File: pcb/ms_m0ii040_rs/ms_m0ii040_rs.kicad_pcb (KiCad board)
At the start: 2 copper layers, 228.6 x 77.7 mm, 100 parts, among them J1 USB_C_Receptacle_USB2.0, J2 Conn_ARM_JTAG_SWD_10, SW1 ESC, SW10 O, SW11 P, SW12 BS, SW13 CTRL, SW14 A, SW15 S, SW16 D, SW17 F, SW18 G, SW19 H, SW2 Q, SW20 J, SW21 K, SW22 L, SW23 ENT, SW25 SHIFT, SW26 Z, SW27 X, SW28 C, SW29 V, SW3 W, SW30 B, SW31 N, SW32 M, SW33 ,, SW34 ., SW35 SHIFT, SW38 WIN, SW39 ALT, SW4 E, SW40 BS, SW42 SPC, SW43 ALT, SW44 APP, SW5 R, SW6 T, SW7 Y, SW8 U, SW9 I, U1 STM32F072C8Tx, U2 TLV73333PDBV

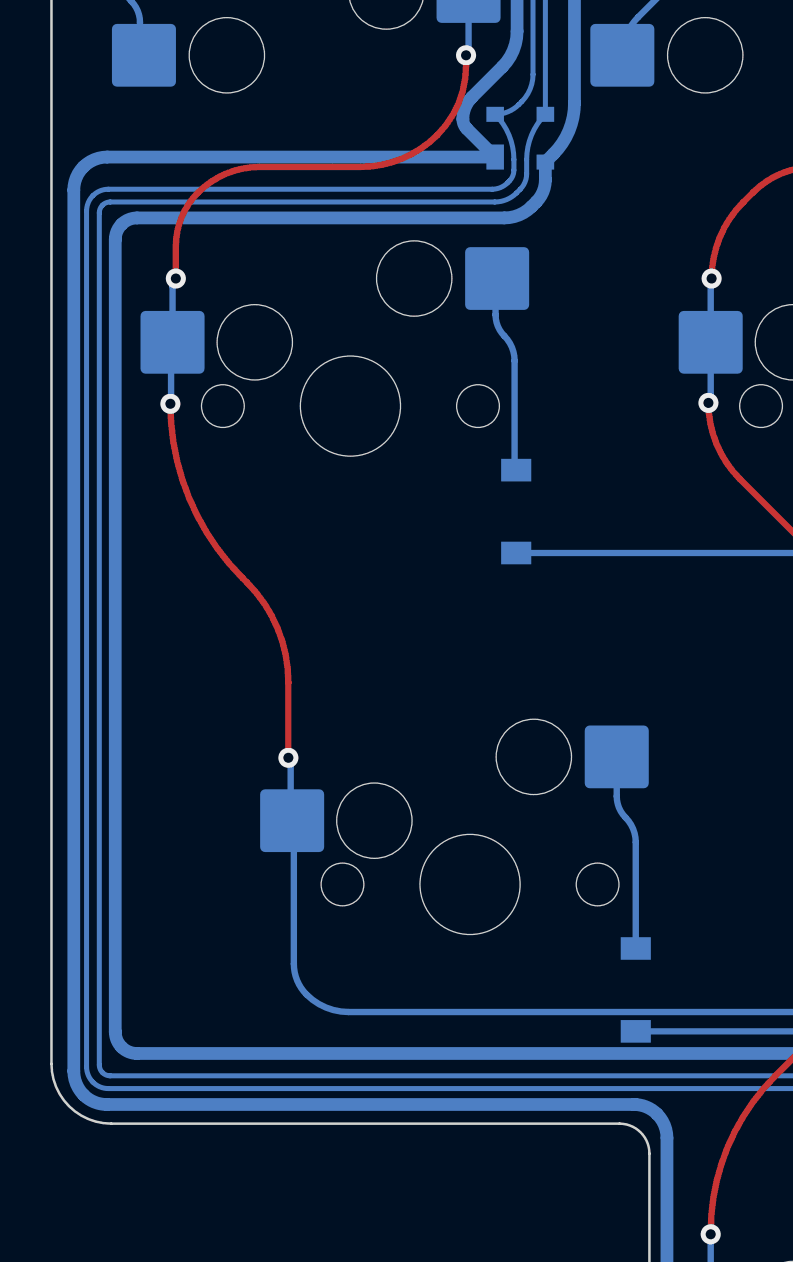
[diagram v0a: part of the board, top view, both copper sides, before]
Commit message: D- and GND slightly separated.
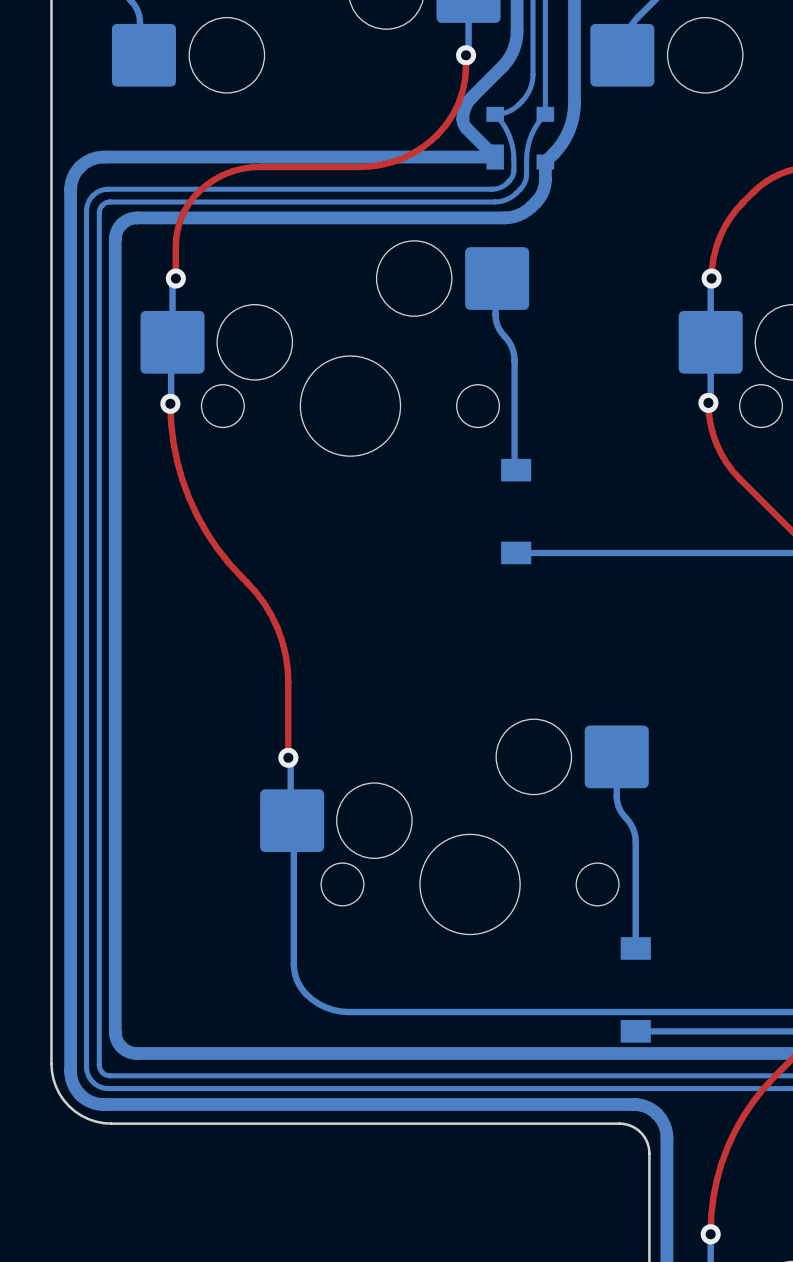
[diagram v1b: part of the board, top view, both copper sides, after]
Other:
- board text added: "M0ii040 Row-staggered rev1.0.2 Copyright marksard 2023. Licensed under CERN-OHL-P v2"
- board text removed: "M0ii040 Row-staggered rev1.0.1 Copyright marksard 2023. Licensed under CERN-OHL-P v2"
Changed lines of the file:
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@@
   (title_block
     (title "m0ii040_rs")
-    (date "2023-03-04")
-    (rev "1.0.1")
+    (date "2023-03-21")
+    (rev "1.0.2")
   )
   (layers
@@
     )
   )
-  (gr_text "M0ii040 Row-staggered rev1.0.1\nCopyright marksard 2023. Licensed under CERN-OHL-P v2\n" (at 215.36025 83.21675) (layer "B.SilkS")
+  (gr_text "M0ii040 Row-staggered rev1.0.2\nCopyright marksard 2023. Licensed under CERN-OHL-P v2\n" (at 215.36025 83.21675) (layer "B.SilkS")
     (effects (font (size 1.5 1.5) (thickness 0.3)) (justify mirror))
   )
@@
   (segment (start 146.474702 111.35995) (end 148.12645 111.35995) (width 0.254) (layer "B.Cu") (net 2))
   (segment (start 139.28725 120.55475) (end 142.93402 120.55475) (width 0.508) (layer "B.Cu") (net 2))
+  (segment (start 48.62525 63.90075) (end 33.048035 63.90075) (width 0.508) (layer "B.Cu") (net 2))
   (segment (start 143.35125 116.84375) (end 143.35125 118.321046) (width 0.508) (layer "B.Cu") (net 2))
   (segment (start 102.177102 110.19155) (end 105.019236 110.19155) (width 0.508) (layer "B.Cu") (net 2))
@@
   (segment (start 134.244447 117.373368) (end 134.104683 117.513132) (width 0.508) (layer "B.Cu") (net 2))
   (segment (start 101.224447 109.796948) (end 101.18725 109.75975) (width 0.508) (layer "B.Cu") (net 2))
-  (segment (start 33.158065 101.63175) (end 54.21904 101.63175) (width 0.508) (layer "B.Cu") (net 2))
   (segment (start 151.8 111.478125) (end 150.680317 111.478125) (width 0.254) (layer "B.Cu") (net 2))
   (segment (start 46.70425 53.37175) (end 46.693052 53.360552) (width 0.508) (layer "B.Cu") (net 2))
@@
   (segment (start 142.93402 120.55475) (end 156.05125 120.55475) (width 0.508) (layer "B.Cu") (net 2))
   (segment (start 145.3875 114.890625) (end 145.3875 112.512983) (width 0.254) (layer "B.Cu") (net 2))
-  (segment (start 48.62525 63.90075) (end 33.175035 63.90075) (width 0.508) (layer "B.Cu") (net 2))
   (segment (start 100.67925 108.53333) (end 100.67925 108.079086) (width 0.508) (layer "B.Cu") (net 2))
   (segment (start 55.46725 119.212965) (end 55.45525 119.224965) (width 0.508) (layer "B.Cu") (net 2))
@@
   (segment (start 151.8 111.478125) (end 153.797191 111.478125) (width 0.254) (layer "B.Cu") (net 2))
   (segment (start 109.129263 120.105737) (end 109.18825 120.04675) (width 0.508) (layer "B.Cu") (net 2))
-  (segment (start 31.84525 65.213565) (end 31.84525 100.301965) (width 0.508) (layer "B.Cu") (net 2))
+  (segment (start 31.71825 65.213565) (end 31.71825 100.301965) (width 0.508) (layer "B.Cu") (net 2))
   (segment (start 149.8875 107.532103) (end 149.8875 106.565625) (width 0.254) (layer "B.Cu") (net 2))
   (segment (start 149.8875 106.565625) (end 149.8875 105.837523) (width 0.254) (layer "B.Cu") (net 2))
@@
   (segment (start 190.34125 118.77675) (end 193.58551 115.53249) (width 0.508) (layer "B.Cu") (net 2))
   (segment (start 100.67925 108.079086) (end 102.673843 108.079086) (width 0.508) (layer "B.Cu") (net 2))
+  (segment (start 33.031065 101.63175) (end 54.21904 101.63175) (width 0.508) (layer "B.Cu") (net 2))
   (segment (start 109.80146 108.23575) (end 141.147841 108.23575) (width 0.508) (layer "B.Cu") (net 2))
   (segment (start 143.475 108.478125) (end 141.732985 108.478125) (width 0.254) (layer "B.Cu") (net 2))
@@
   (arc (start 153.797191 111.478125) (mid 153.848637 111.467891) (end 153.89225 111.43875) (width 0.254) (layer "B.Cu") (net 2))
   (arc (start 141.147841 108.23575) (mid 141.240606 108.254203) (end 141.31925 108.30675) (width 0.508) (layer "B.Cu") (net 2))
-  (arc (start 31.84525 100.301965) (mid 31.947388 100.815444) (end 32.23825 101.25075) (width 0.508) (layer "B.Cu") (net 2))
-  (arc (start 32.22625 64.29375) (mid 31.944276 64.715765) (end 31.84525 65.213565) (width 0.508) (layer "B.Cu") (net 2))
+  (arc (start 31.71825 100.301965) (mid 31.820388 100.815444) (end 32.11125 101.25075) (width 0.508) (layer "B.Cu") (net 2))
+  (arc (start 32.09925 64.29375) (mid 31.817276 64.715765) (end 31.71825 65.213565) (width 0.508) (layer "B.Cu") (net 2))
   (arc (start 183.514065 116.74475) (mid 184.279439 116.592508) (end 184.928291 116.158958) (width 0.508) (layer "B.Cu") (net 2))
   (arc (start 140.90202 120.55475) (mid 141.897621 120.356712) (end 142.74165 119.79275) (width 0.508) (layer "B.Cu") (net 2))
@@
   (arc (start 149.19325 110.85195) (mid 149.34364 110.626875) (end 149.39645 110.361382) (width 0.254) (layer "B.Cu") (net 2))
   (arc (start 141.732985 108.478125) (mid 141.509073 108.433586) (end 141.31925 108.30675) (width 0.254) (layer "B.Cu") (net 2))
-  (arc (start 32.23825 101.25075) (mid 32.660265 101.532735) (end 33.158065 101.63175) (width 0.508) (layer "B.Cu") (net 2))
+  (arc (start 32.11125 101.25075) (mid 32.533265 101.532735) (end 33.031065 101.63175) (width 0.508) (layer "B.Cu") (net 2))
   (arc (start 138.429065 120.04675) (mid 138.147083 119.624735) (end 138.048065 119.126935) (width 0.508) (layer "B.Cu") (net 2))
   (arc (start 149.70125 107.98175) (mid 149.839096 107.77545) (end 149.8875 107.532103) (width 0.254) (layer "B.Cu") (net 2))
@@
   (arc (start 187.225237 119.089737) (mid 187.722586 119.422055) (end 188.30925 119.53875) (width 0.508) (layer "B.Cu") (net 2))
   (arc (start 109.56925 119.03075) (mid 109.732622 118.209421) (end 110.197868 117.513132) (width 0.508) (layer "B.Cu") (net 2))
-  (arc (start 33.175035 63.90075) (mid 32.661556 64.002888) (end 32.22625 64.29375) (width 0.508) (layer "B.Cu") (net 2))
+  (arc (start 33.048035 63.90075) (mid 32.534556 64.002888) (end 32.09925 64.29375) (width 0.508) (layer "B.Cu") (net 2))
   (arc (start 145.12925 116.49075) (mid 144.738249 116.752009) (end 144.277033 116.84375) (width 0.254) (layer "B.Cu") (net 2))
   (arc (start 45.68625 50.929919) (mid 45.84316 51.718756) (end 46.29 52.3875) (width 0.508) (layer "B.Cu") (net 2))
